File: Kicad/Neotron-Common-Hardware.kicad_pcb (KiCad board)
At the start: 2 copper layers, 170 x 175 mm, 8 parts, among them J101 DB15_Female_HighDensity_Mount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, J103 DB9_Male_MountingHoles, J106 RJ45_Amphenol_RJMG1BD3B8K1ANR, J107 Double-mini-DIN-6

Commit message: Fixing up hole locations on the PCB.
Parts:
- removed G***: LOGO, Neotron-Common-Hardware:logo_small
- removed the REF** at (205.5, 99.0)
- added REF**: PinSocket_2x16_P2.54mm_Vertical, Connector_PinSocket_2.54mm:PinSocket_2x16_P2.54mm_Vertical, F.Cu at (55.8, 54.0)
- added REF**: MountingHole_4.3mm_M4_Pad_Via, MountingHole:MountingHole_4.3mm_M4_Pad_Via, F.Cu at (113.8, 41.3)
- added REF**: MountingHole_4.3mm_M4_Pad_Via, MountingHole:MountingHole_4.3mm_M4_Pad_Via, F.Cu at (57.9, 41.3)
- added REF**: PinSocket_2x16_P2.54mm_Vertical, Connector_PinSocket_2.54mm:PinSocket_2x16_P2.54mm_Vertical, F.Cu at (76.1, 54.0)
- added REF**: PinSocket_2x16_P2.54mm_Vertical, Connector_PinSocket_2.54mm:PinSocket_2x16_P2.54mm_Vertical, F.Cu at (96.4, 54.0)
- added REF**: PinSocket_2x16_P2.54mm_Vertical, Connector_PinSocket_2.54mm:PinSocket_2x16_P2.54mm_Vertical, F.Cu at (116.8, 54.0)
- added REF**: MountingHole_4.3mm_M4_Pad_Via, MountingHole:MountingHole_4.3mm_M4_Pad_Via, F.Cu at (113.8, 196.3)
- added REF**: MountingHole_4.3mm_M4_Pad_Via, MountingHole:MountingHole_4.3mm_M4_Pad_Via, F.Cu at (271.2, 64.2)
- added REF**: MountingHole_4.3mm_M4_Pad_Via, MountingHole:MountingHole_4.3mm_M4_Pad_Via, F.Cu at (271.2, 268.7)
- added REF**: MountingHole_4.3mm_M4_Pad_Via, MountingHole:MountingHole_4.3mm_M4_Pad_Via, F.Cu at (271.2, 196.3)
- added REF**: MountingHole_4.3mm_M4_Pad_Via, MountingHole:MountingHole_4.3mm_M4_Pad_Via, F.Cu at (113.8, 268.7)
- moved J107 66.6 mm to (265.7, 42.1)
- moved J101 65.8 mm to (226.0, 38.7)
- moved J103 65.8 mm to (194.2, 39.3)
- moved J106 65.8 mm to (166.9, 48.2)
- moved REF** 65.8 mm to (144.2, 38.1)
- moved REF** 65.5 mm to (250.9, 47.1)
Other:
- board size 170 x 175 mm -> 243.8 x 243.8 mm
- board text added: "Neotron Expansion Slots Use right-angle double header fitted to 'top' side of card. See RS 251-8496."
- board text added: "micro-ATX outline"
- board text added: "micro-ATX short outline"
- board text added: "micro-ITX outline"
- board text removed: "Example ATX Board"
- board text removed: "https://github.com/neotron-compute"

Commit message: Brought in RS232 circuit from Neotron 32.
Also updated 3D models.
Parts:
- removed J101: DB15_Female_HighDensity_MountingHoles, Connector_Dsub:DSUB-15-HD_Male_Horizontal_P2.29x1.98mm_EdgePinOffset3.03mm_Housed_MountingHolesOffset4.94mm
- removed J103: DB9_Male_MountingHoles, Connector_Dsub:DSUB-9_Male_Horizontal_P2.77x2.84mm_EdgePinOffset4.94mm_Housed_MountingHolesOffset7.48mm
- removed J106: RJ45_Amphenol_RJMG1BD3B8K1ANR, Connector_RJ:RJ45_Amphenol_RJMG1BD3B8K1ANR
- removed J107: Double-mini-DIN-6, Neotron-Common-Hardware:Double_mini-DIN_6
- removed REF** (x4): PinSocket_2x16_P2.54mm_Vertical, Connector_PinSocket_2.54mm:PinSocket_2x16_P2.54mm_Vertical
- removed REF** (x7): MountingHole_4.3mm_M4_Pad_Via, MountingHole:MountingHole_4.3mm_M4_Pad_Via
- removed REF**: STX-4335-5BGP-S1, Neotron-Common-Hardware:STX-4335-5BGP-S1
- removed REF**: USB_A_Wuerth_61400826021_Horizontal_Stacked, Connector_USB:USB_A_Wuerth_61400826021_Horizontal_Stacked
- added C801: 100n, Capacitor_THT:C_Disc_D3.0mm_W2.0mm_P2.50mm, F.Cu at (205.8, 61.0)
- added C802: 100n, Capacitor_THT:C_Disc_D3.0mm_W2.0mm_P2.50mm, F.Cu at (205.8, 68.1)
- added C803: 100n, Capacitor_THT:C_Disc_D3.0mm_W2.0mm_P2.50mm, F.Cu at (193.8, 58.0)
- added C804: 100n, Capacitor_THT:C_Disc_D3.0mm_W2.0mm_P2.50mm, F.Cu at (205.8, 64.6)
- added C805: 100n, Capacitor_THT:C_Disc_D3.0mm_W2.0mm_P2.50mm, F.Cu at (211.4, 64.0)
- added FB401: 220R@100MHz, Inductor_SMD:L_0805_2012Metric_Pad1.15x1.40mm_HandSolder, F.Cu at (170.1, 82.8)
- added FB402: 220R@100MHz, Inductor_SMD:L_0805_2012Metric_Pad1.15x1.40mm_HandSolder, F.Cu at (174.6, 77.4)
- added FB403: 220R@100MHz, Inductor_SMD:L_0805_2012Metric_Pad1.15x1.40mm_HandSolder, F.Cu at (165.3, 82.8)
- added FB404: 220R@100MHz, Inductor_SMD:L_0805_2012Metric_Pad1.15x1.40mm_HandSolder, F.Cu at (173.9, 74.5)
- added FB405: 220R@100MHz, Inductor_SMD:L_0805_2012Metric_Pad1.15x1.40mm_HandSolder, F.Cu at (169.9, 79.8)
- added FB406: 220R@100MHz, Inductor_SMD:L_0805_2012Metric_Pad1.15x1.40mm_HandSolder, F.Cu at (148.6, 83.3)
- added FB407: 220R@100MHz, Inductor_SMD:L_0805_2012Metric_Pad1.15x1.40mm_HandSolder, F.Cu at (173.9, 71.5)
- added FB408: 220R@100MHz, Inductor_SMD:L_0805_2012Metric_Pad1.15x1.40mm_HandSolder, F.Cu at (160.6, 82.8)
- added FB409: 600R@100MHz, Inductor_SMD:L_0805_2012Metric_Pad1.15x1.40mm_HandSolder, F.Cu at (173.9, 68.5)
- added FB410: 220R@100MHz, Inductor_SMD:L_0805_2012Metric_Pad1.15x1.40mm_HandSolder, F.Cu at (165.1, 79.8)
- added FB411: 220R@100MHz, Inductor_SMD:L_0805_2012Metric_Pad1.15x1.40mm_HandSolder, F.Cu at (155.8, 80.8)
- added J201: DB15_Female_HighDensity_MountingHoles, Connector_Dsub:DSUB-15-HD_Male_Horizontal_P2.29x1.98mm_EdgePinOffset3.03mm_Housed_MountingHolesOffset4.94mm, F.Cu at (228.8, 39.0)
- added J301: RJ45_Amphenol_RJMG1BD3B8K1ANR, Connector_RJ:RJ45_Amphenol_RJMG1BD3B8K1ANR, F.Cu at (170.8, 49.0)
- added J401: CD Audio In, Connector_PinHeader_2.54mm:PinHeader_1x04_P2.54mm_Vertical, F.Cu at (150.8, 66.0)
- added J402: AC'97 Audio Header, Connector_PinHeader_2.54mm:PinHeader_2x05_P2.54mm_Vertical, F.Cu at (143.8, 66.0)
- added J403: Line Out, Connector_PinHeader_2.54mm:PinHeader_1x04_P2.54mm_Vertical, F.Cu at (154.8, 66.0)
- added J501: USB_A, Connector_USB:USB_A_Stewart_SS-52100-001_Horizontal, F.Cu at (252.8, 44.0)
- added J601: USB_B, Connector_USB:USB_B_OST_USB-B1HSxx_Horizontal, F.Cu at (130.8, 46.0)
- added J701: Double-mini-DIN-6, Neotron-Common-Hardware:Double_mini-DIN_6, F.Cu at (265.8, 42.0)
- added J801: Conn_02x05, Connector_IDC:IDC-Header_2x05_P2.54mm_Vertical, F.Cu at (197.8, 50.0)
- added J802: DB9_Male_MountingHoles, Connector_Dsub:DSUB-9_Male_Horizontal_P2.77x2.84mm_EdgePinOffset4.94mm_Housed_MountingHolesOffset7.48mm, F.Cu at (198.0, 39.8)
- added U401: TLV320AIC23BPW, Package_SO:TSSOP-28_4.4x9.7mm_P0.65mm, F.Cu at (165.8, 70.0)
- added U402: STX-4335-5BGP-S1, Neotron-Common-Hardware:STX-4335-5BGP-S1, F.Cu at (148.8, 39.0)
- added U801: ICL3232CPZMAX, Package_DIP:DIP-16_W7.62mm, F.Cu at (201.8, 61.0)

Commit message: Add ATX/ITX mounting holes.
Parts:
- removed the FB407 at (173.9, 71.5)
- removed the FB408 at (160.6, 82.8)
- added C301: 100n, Capacitor_SMD:C_0805_2012Metric_Pad1.15x1.40mm_HandSolder, F.Cu at (175.8, 75.0)
- added C302: 100n, Capacitor_SMD:C_0805_2012Metric_Pad1.15x1.40mm_HandSolder, F.Cu at (163.2, 71.4)
- added C303: 100n, Capacitor_SMD:C_0805_2012Metric_Pad1.15x1.40mm_HandSolder, F.Cu at (169.9, 76.5)
- added C304: 100n, Capacitor_SMD:C_0805_2012Metric_Pad1.15x1.40mm_HandSolder, F.Cu at (166.2, 71.4)
- added C305: 100n, Capacitor_SMD:C_0805_2012Metric_Pad1.15x1.40mm_HandSolder, F.Cu at (163.2, 66.6)
- added C306: 1n, Capacitor_SMD:C_0805_2012Metric_Pad1.15x1.40mm_HandSolder, F.Cu at (172.8, 76.5)
- added C307: 1n, Capacitor_SMD:C_0805_2012Metric_Pad1.15x1.40mm_HandSolder, F.Cu at (177.7, 79.8)
- added C308: 10u Low ESR, Capacitor_THT:CP_Radial_D6.3mm_P2.50mm, F.Cu at (172.3, 84.1)
- added C309: 12p, Capacitor_SMD:C_0805_2012Metric_Pad1.15x1.40mm_HandSolder, F.Cu at (169.1, 71.4)
- added C310: 10n, Capacitor_SMD:C_0805_2012Metric_Pad1.15x1.40mm_HandSolder, F.Cu at (166.2, 66.6)
- added C311: 10n, Capacitor_SMD:C_0805_2012Metric_Pad1.15x1.40mm_HandSolder, F.Cu at (163.2, 61.9)
- added C312: 12p, Capacitor_SMD:C_0805_2012Metric_Pad1.15x1.40mm_HandSolder, F.Cu at (172.1, 71.8)
- added C401: 22p, Capacitor_SMD:C_0805_2012Metric_Pad1.15x1.40mm_HandSolder, F.Cu at (177.8, 113.0)
- added C402: 10u, Capacitor_THT:CP_Radial_D6.3mm_P2.50mm, F.Cu at (178.4, 95.9)
- added C403: 10u, Capacitor_THT:CP_Radial_D6.3mm_P2.50mm, F.Cu at (151.7, 115.7)
- added C404: 10u, Capacitor_THT:CP_Radial_D6.3mm_P2.50mm, F.Cu at (165.0, 103.8)
- added C405: 22p, Capacitor_SMD:C_0805_2012Metric_Pad1.15x1.40mm_HandSolder, F.Cu at (164.1, 117.3)
- added C406: 100n, Capacitor_SMD:C_0805_2012Metric_Pad1.15x1.40mm_HandSolder, F.Cu at (179.8, 101.6)
- added C407: 10u, Capacitor_THT:CP_Radial_D6.3mm_P2.50mm, F.Cu at (138.4, 122.8)
- added C408: 100n, Capacitor_SMD:C_0805_2012Metric_Pad1.15x1.40mm_HandSolder, F.Cu at (149.8, 129.2)
- added C409: 10u, Capacitor_THT:CP_Radial_D6.3mm_P2.50mm, F.Cu at (130.4, 122.8)
- added C410: 10u, Capacitor_THT:CP_Radial_D6.3mm_P2.50mm, F.Cu at (143.8, 111.9)
- added C411: 100n, Capacitor_SMD:C_0805_2012Metric_Pad1.15x1.40mm_HandSolder, F.Cu at (166.5, 113.0)
- added C412: 10u, Capacitor_THT:CP_Radial_D6.3mm_P2.50mm, F.Cu at (157.1, 100.0)
- added C413: 100n, Capacitor_SMD:C_0805_2012Metric_Pad1.15x1.40mm_HandSolder, F.Cu at (166.5, 109.5)
- added C414: 10u, Capacitor_THT:CP_Radial_D6.3mm_P2.50mm, F.Cu at (170.4, 95.9)
- added C415: 10u, Capacitor_THT:CP_Radial_D6.3mm_P2.50mm, F.Cu at (159.7, 111.6)
- added C416: 100n, Capacitor_SMD:C_0805_2012Metric_Pad1.15x1.40mm_HandSolder, F.Cu at (127.2, 128.5)
- added C417: 10u, Capacitor_THT:CP_Radial_D6.3mm_P2.50mm, F.Cu at (143.8, 104.0)
- added C418: 470n, Capacitor_SMD:C_0805_2012Metric_Pad1.15x1.40mm_HandSolder, F.Cu at (158.5, 117.3)
- added C419: 470n, Capacitor_SMD:C_0805_2012Metric_Pad1.15x1.40mm_HandSolder, F.Cu at (144.2, 129.2)
- added C420: 220u, Capacitor_THT:CP_Radial_D6.3mm_P2.50mm, F.Cu at (154.4, 123.5)
- added C421: 220u, Capacitor_THT:CP_Radial_D6.3mm_P2.50mm, F.Cu at (173.0, 103.8)
- added C422: 470n, Capacitor_SMD:C_0805_2012Metric_Pad1.15x1.40mm_HandSolder, F.Cu at (138.5, 128.5)
- added C423: 470n, Capacitor_SMD:C_0805_2012Metric_Pad1.15x1.40mm_HandSolder, F.Cu at (132.8, 128.5)
- added C424: DNF, Capacitor_SMD:C_0805_2012Metric_Pad1.15x1.40mm_HandSolder, F.Cu at (121.5, 129.7)
- added C425: 1u, Capacitor_THT:CP_Radial_D6.3mm_P2.50mm, F.Cu at (146.4, 123.5)
- added C426: DNF, Capacitor_SMD:C_0805_2012Metric_Pad1.15x1.40mm_HandSolder, F.Cu at (121.5, 126.2)
- added C427: DNF, Capacitor_SMD:C_0805_2012Metric_Pad1.15x1.40mm_HandSolder, F.Cu at (115.9, 129.7)
- added C428: DNF, Capacitor_SMD:C_0805_2012Metric_Pad1.15x1.40mm_HandSolder, F.Cu at (115.9, 126.2)
- added C429: 47p, Capacitor_SMD:C_0805_2012Metric_Pad1.15x1.40mm_HandSolder, F.Cu at (151.7, 107.8)
- added C430: DNF, Capacitor_SMD:C_0805_2012Metric_Pad1.15x1.40mm_HandSolder, F.Cu at (172.1, 109.5)
- added C431: DNF, Capacitor_SMD:C_0805_2012Metric_Pad1.15x1.40mm_HandSolder, F.Cu at (166.8, 120.9)
- added C432: DNF, Capacitor_SMD:C_0805_2012Metric_Pad1.15x1.40mm_HandSolder, F.Cu at (177.8, 109.5)
- added C433: DNF, Capacitor_SMD:C_0805_2012Metric_Pad1.15x1.40mm_HandSolder, F.Cu at (169.8, 116.6)
- added C434: DNF, Capacitor_SMD:C_0805_2012Metric_Pad1.15x1.40mm_HandSolder, F.Cu at (161.1, 124.4)
- added C435: DNF, Capacitor_SMD:C_0805_2012Metric_Pad1.15x1.40mm_HandSolder, F.Cu at (155.4, 129.2)
- added C436: DNF, Capacitor_SMD:C_0805_2012Metric_Pad1.15x1.40mm_HandSolder, F.Cu at (179.8, 105.2)
- added C437: DNF, Capacitor_SMD:C_0805_2012Metric_Pad1.15x1.40mm_HandSolder, F.Cu at (172.1, 113.0)
- added C438: DNF, Capacitor_SMD:C_0805_2012Metric_Pad1.15x1.40mm_HandSolder, F.Cu at (161.1, 120.9)
- added FB406: 220R@100MHz, Inductor_SMD:L_0805_2012Metric_Pad1.15x1.40mm_HandSolder, F.Cu at (143.2, 117.3)
- added FB410: 220R@100MHz, Inductor_SMD:L_0805_2012Metric_Pad1.15x1.40mm_HandSolder, F.Cu at (151.3, 101.6)
- added H101: MountingHole_Pad, MountingHole:MountingHole_4.3mm_M4_Pad_Via, F.Cu at (68.0, 41.3)
- added H102: MountingHole_Pad, MountingHole:MountingHole_4.3mm_M4_Pad_Via, F.Cu at (68.0, 196.3)
- added H103: MountingHole_Pad, MountingHole:MountingHole_4.3mm_M4_Pad_Via, F.Cu at (113.8, 41.3)
- added H104: MountingHole_Pad, MountingHole:MountingHole_4.3mm_M4_Pad_Via, F.Cu at (113.8, 196.3)
- added H105: MountingHole_Pad, MountingHole:MountingHole_4.3mm_M4_Pad_Via, F.Cu at (271.2, 64.2)
- added H106: MountingHole_Pad, MountingHole:MountingHole_4.3mm_M4_Pad_Via, F.Cu at (113.8, 268.7)
- added H107: MountingHole_Pad, MountingHole:MountingHole_4.3mm_M4_Pad_Via, F.Cu at (271.2, 268.7)
- added H108: MountingHole_Pad, MountingHole:MountingHole_4.3mm_M4_Pad_Via, F.Cu at (47.7, 196.3)
- added H109: MountingHole_Pad, MountingHole:MountingHole_4.3mm_M4_Pad_Via, F.Cu at (271.2, 196.3)
- added J901: DB9_Female_MountingHoles, Connector_Dsub:DSUB-9_Female_Horizontal_P2.77x2.84mm_EdgePinOffset4.94mm_Housed_MountingHolesOffset7.48mm, F.Cu at (252.1, 267.0)
- added R301: 100k, Resistor_SMD:R_0805_2012Metric_Pad1.15x1.40mm_HandSolder, F.Cu at (177.7, 84.5)
- added R302: 49R9 1%, Resistor_SMD:R_0805_2012Metric_Pad1.15x1.40mm_HandSolder, F.Cu at (169.1, 66.6)
- added R303: 49R9 1%, Resistor_SMD:R_0805_2012Metric_Pad1.15x1.40mm_HandSolder, F.Cu at (166.2, 61.9)
- added R304: 49R9 1%, Resistor_SMD:R_0805_2012Metric_Pad1.15x1.40mm_HandSolder, F.Cu at (172.1, 67.0)
- added R305: 49R9 1%, Resistor_SMD:R_0805_2012Metric_Pad1.15x1.40mm_HandSolder, F.Cu at (175.0, 70.3)
- added R306: 12k4 1%, Resistor_SMD:R_0805_2012Metric_Pad1.15x1.40mm_HandSolder, F.Cu at (169.1, 61.9)
- added R307: 1M, Resistor_SMD:R_0805_2012Metric_Pad1.15x1.40mm_HandSolder, F.Cu at (178.0, 70.3)
- added R308: 10, Resistor_SMD:R_0805_2012Metric_Pad1.15x1.40mm_HandSolder, F.Cu at (172.1, 62.3)
- added R309: 10, Resistor_SMD:R_0805_2012Metric_Pad1.15x1.40mm_HandSolder, F.Cu at (175.0, 65.5)
- added R310: 180, Resistor_SMD:R_0805_2012Metric_Pad1.15x1.40mm_HandSolder, F.Cu at (178.0, 65.5)
- added R311: 180, Resistor_SMD:R_0805_2012Metric_Pad1.15x1.40mm_HandSolder, F.Cu at (172.1, 57.5)
- added R312: DNF, Resistor_SMD:R_0805_2012Metric_Pad1.15x1.40mm_HandSolder, F.Cu at (175.0, 60.8)
- added R401: 2R2, Resistor_SMD:R_0805_2012Metric_Pad1.15x1.40mm_HandSolder, F.Cu at (155.8, 94.0)
- added R402: 2R2, Resistor_SMD:R_0805_2012Metric_Pad1.15x1.40mm_HandSolder, F.Cu at (129.2, 110.2)
- added R403: 2R2, Resistor_SMD:R_0805_2012Metric_Pad1.15x1.40mm_HandSolder, F.Cu at (129.2, 106.2)
- added R404: 100, Resistor_SMD:R_0805_2012Metric_Pad1.15x1.40mm_HandSolder, F.Cu at (115.9, 94.0)
- added R405: 100, Resistor_SMD:R_0805_2012Metric_Pad1.15x1.40mm_HandSolder, F.Cu at (115.9, 122.4)
- added R406: 47k, Resistor_SMD:R_0805_2012Metric_Pad1.15x1.40mm_HandSolder, F.Cu at (142.5, 98.1)
- added R407: 47k, Resistor_SMD:R_0805_2012Metric_Pad1.15x1.40mm_HandSolder, F.Cu at (115.9, 118.3)
- added R408: 4k7, Resistor_SMD:R_0805_2012Metric_Pad1.15x1.40mm_HandSolder, F.Cu at (129.2, 102.1)
- added R409: 47k, Resistor_SMD:R_0805_2012Metric_Pad1.15x1.40mm_HandSolder, F.Cu at (115.9, 114.3)
- added R410: 47k, Resistor_SMD:R_0805_2012Metric_Pad1.15x1.40mm_HandSolder, F.Cu at (142.5, 94.0)
- added R411: 2k2, Resistor_SMD:R_0805_2012Metric_Pad1.15x1.40mm_HandSolder, F.Cu at (115.9, 110.2)
- added R412: 4k7, Resistor_SMD:R_0805_2012Metric_Pad1.15x1.40mm_HandSolder, F.Cu at (115.9, 106.2)
- added R413: 4k7, Resistor_SMD:R_0805_2012Metric_Pad1.15x1.40mm_HandSolder, F.Cu at (129.2, 98.1)
- added R414: 4k7, Resistor_SMD:R_0805_2012Metric_Pad1.15x1.40mm_HandSolder, F.Cu at (115.9, 102.1)
- added R415: 4k7, Resistor_SMD:R_0805_2012Metric_Pad1.15x1.40mm_HandSolder, F.Cu at (129.2, 94.0)
- added R416: 10k, Resistor_SMD:R_0805_2012Metric_Pad1.15x1.40mm_HandSolder, F.Cu at (115.9, 98.1)
- added R801: DNF, Resistor_SMD:R_0805_2012Metric_Pad1.15x1.40mm_HandSolder, F.Cu at (115.9, 136.9)
- added U301: ENC424J600-PT, Package_QFP:TQFP-44_10x10mm_P0.8mm, F.Cu at (187.8, 82.0)
- added Y301: 25M, Crystal:Crystal_HC49-4H_Vertical, F.Cu at (165.1, 82.8)
- added Y401: 12M, Crystal:Crystal_HC49-4H_Vertical, F.Cu at (131.8, 115.6)
- C801, C802, C803, C804, C805: footprint Capacitor_THT:C_Disc_D3.0mm_W2.0mm_P2.50mm -> Capacitor_SMD:C_0805_2012Metric_Pad1.15x1.40mm_HandSolder
- U801: value ICL3232CPZMAX -> ST3232CDR; footprint Package_DIP:DIP-16_W7.62mm -> Package_SO:SOP-16_4.4x10.4mm_P1.27mm
- moved FB402 22.0 mm to (155.8, 66.0)
- moved FB404 22.0 mm to (155.8, 62.0)
- moved FB407 20.9 mm to (155.8, 58.0)
- moved C804 20.3 mm to (185.8, 61.0), turned to 90 degrees
- moved U401 17.5 mm to (148.8, 74.0)
- moved FB401 15.8 mm to (155.1, 87.8)
- moved FB403 15.8 mm to (150.3, 87.8)
- moved FB405 15.8 mm to (154.9, 84.8)
- moved FB408 15.8 mm to (150.1, 84.8)
- moved FB409 15.8 mm to (133.6, 88.3)
- moved FB411 15.8 mm to (140.8, 85.8)
- moved C802 14.2 mm to (195.8, 58.0)
- moved C801 12.7 mm to (196.8, 70.0)
- moved C805 12.0 mm to (199.8, 61.0), turned to 90 degrees
- moved J401 11.2 mm to (145.8, 56.0)
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- renumbered FB409 to FB407, FB410 to FB408, FB406 to FB409
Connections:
- FB401 pad 1: (no net) -> Net-(C403-Pad1)
- FB402 pad 1: (no net) -> Net-(C404-Pad1)
- FB403 pad 1: (no net) -> Net-(C414-Pad1)
- FB405 pad 2: (no net) -> Net-(C424-Pad2)
- FB407 pad 2: (no net) -> Net-(C425-Pad2)
- FB408 pad 2: (no net) -> Net-(C430-Pad2)
- FB409 pad 2: (no net) -> Net-(C431-Pad2)
- FB411 pad 2: (no net) -> Net-(C436-Pad2)
- J301 pad L1: (no net) -> Net-(J301-PadL1)
- J301 pad L2: (no net) -> GND
- J301 pad L3: (no net) -> GND
- J301 pad L4: (no net) -> Net-(J301-PadL4)
- J301 pad R1: (no net) -> Net-(J301-PadR1)
- J301 pad R2: (no net) -> Net-(J301-PadR2)
- J301 pad R3: (no net) -> Net-(J301-PadR3)
- J301 pad R4: (no net) -> Net-(C310-Pad1)
- J301 pad R5: (no net) -> Net-(C311-Pad1)
- J301 pad R6: (no net) -> Net-(J301-PadR6)
- J301 pad R8: (no net) -> GND
- J402 pad 7: (no net) -> /Audio/5V0_ANALOG
- U401 pad 10: (no net) -> Net-(C421-Pad1)
- U401 pad 12: (no net) -> Net-(C418-Pad1)
- U401 pad 13: (no net) -> Net-(C419-Pad1)
- U401 pad 16: (no net) -> Net-(C415-Pad1)
- U401 pad 17: (no net) -> /Audio/BIASOUT
- U401 pad 18: (no net) -> /Audio/MICIN
- U401 pad 19: (no net) -> Net-(C423-Pad1)
- U401 pad 20: (no net) -> Net-(C422-Pad1)
- U401 pad 25: (no net) -> Net-(C401-Pad2)
- U401 pad 26: (no net) -> Net-(C405-Pad1)
- U401 pad 9: (no net) -> Net-(C420-Pad1)
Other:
- board text added: "micro-ATX outline (244mm x 244mm)"
- board text added: "micro-ATX short outline (244mm x 170mm)"
- board text added: "micro-ITX outline (170mm x 170mm)"
- board text removed: "micro-ATX outline"
- board text removed: "micro-ATX short outline"
- board text removed: "micro-ITX outline"

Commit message: Add logos
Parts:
- added LOGO101: OSHW Logo, Symbol:OSHW-Logo_11.4x12mm_SilkScreen, F.Cu at (258.6, 192.5)
- added LOGO102: Kicad Logo, Symbol:KiCad-Logo2_12mm_SilkScreen, F.Cu at (235.7, 189.9)
- added LOGO103: Neotron Logo, Neotron-Common-Hardware:logo, F.Cu at (233.2, 55.3)
- renumbered H103 to H102, H105 to H103, H108 to H104, H102 to H105, H104 to H106, H109 to H107, H106 to H108, H107 to H109
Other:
- board text added: "PCB Version: [Uncontrolled]"
- board text added: "https://neotron-compute.github.io"

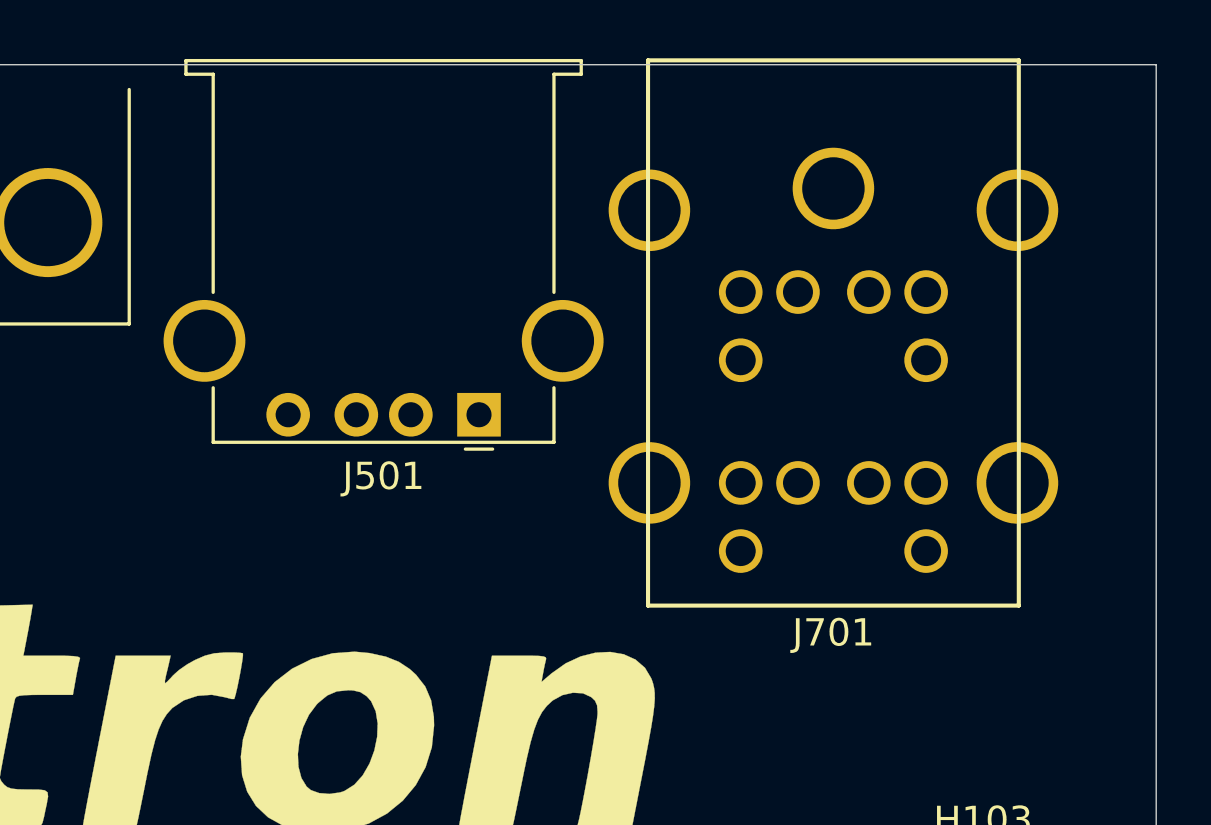
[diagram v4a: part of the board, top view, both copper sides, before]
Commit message: Added dual Type-A USB header.
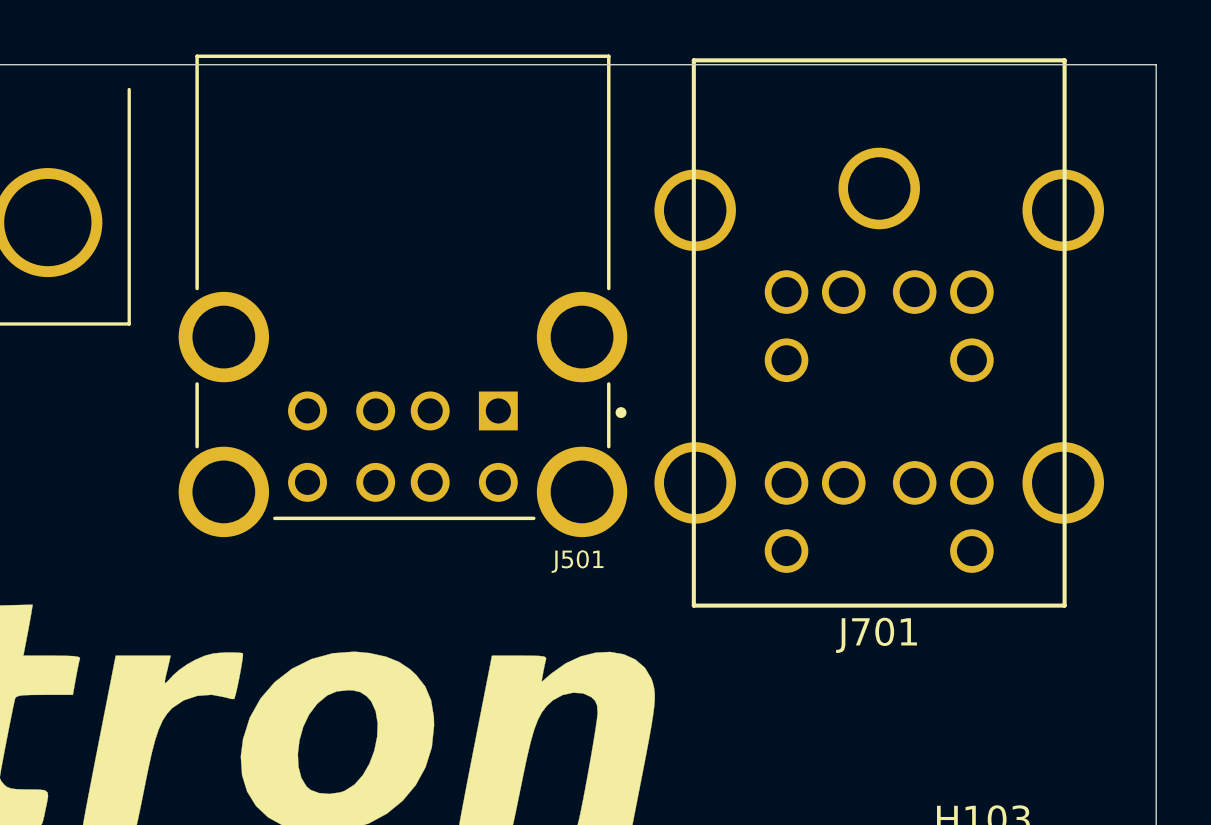
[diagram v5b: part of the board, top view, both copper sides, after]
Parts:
- J501: value USB_A -> USB_A_x2; footprint Connector_USB:USB_A_Stewart_SS-52100-001_Horizontal -> Neotron-Common-Hardware:CUI_UJ2-ADH-1-TH
- moved J701 1.68 mm to (267.4, 42.0)
- moved J501 0.72 mm to (253.5, 43.9)
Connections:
- J501 pad 5: Net-(J501-Pad5) -> (no net)
